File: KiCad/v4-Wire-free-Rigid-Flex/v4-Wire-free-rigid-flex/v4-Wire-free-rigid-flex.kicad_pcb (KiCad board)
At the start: 6 copper layers, 28.5 x 27 mm, 90 parts, among them J1 0475710001, J11 Conn_01x01, J12 Conn_01x01, J13 Conn_01x01, J2 Conn_01x01, J4 Conn_01x01, J5 Conn_01x01, J6 Conn_01x01, J7 Conn_01x01, J8 Conn_01x01, J9 Conn_01x01, Q1 MMBT3904LP-7B, U1 TPS62402-Q1, U2 LTC3218, U2 MAX13030EETE+, U3 ATSAME70N21A-CN, U3 TPL0102-100RUCR, U4 MAX14574EWL+, U5 LMV321IDCKR, U6 NOIP1SN0480A, U7 SiT_2.5mmx2mm, Y1 ABM8G-12.000MHZ-4Y-T3

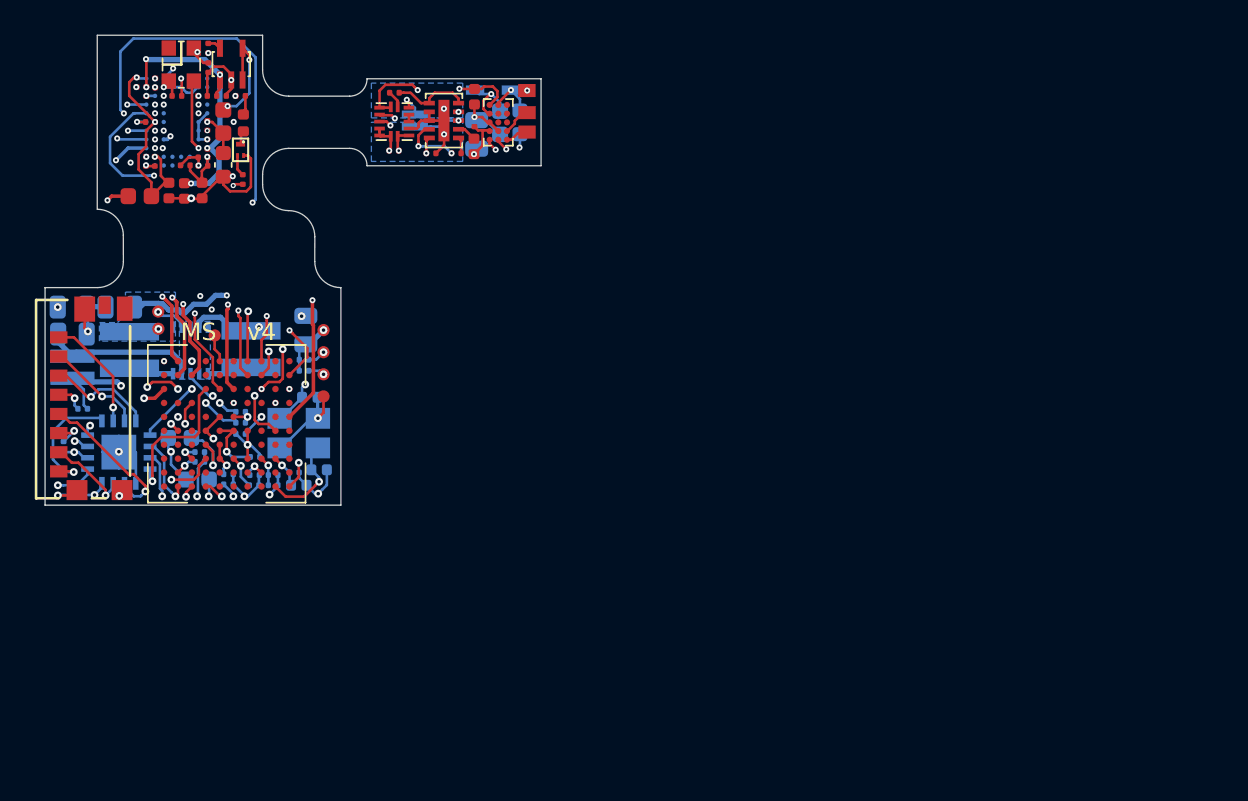
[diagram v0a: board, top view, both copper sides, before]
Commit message: Rigid-flex first draft
To do: Arrange the screw holes
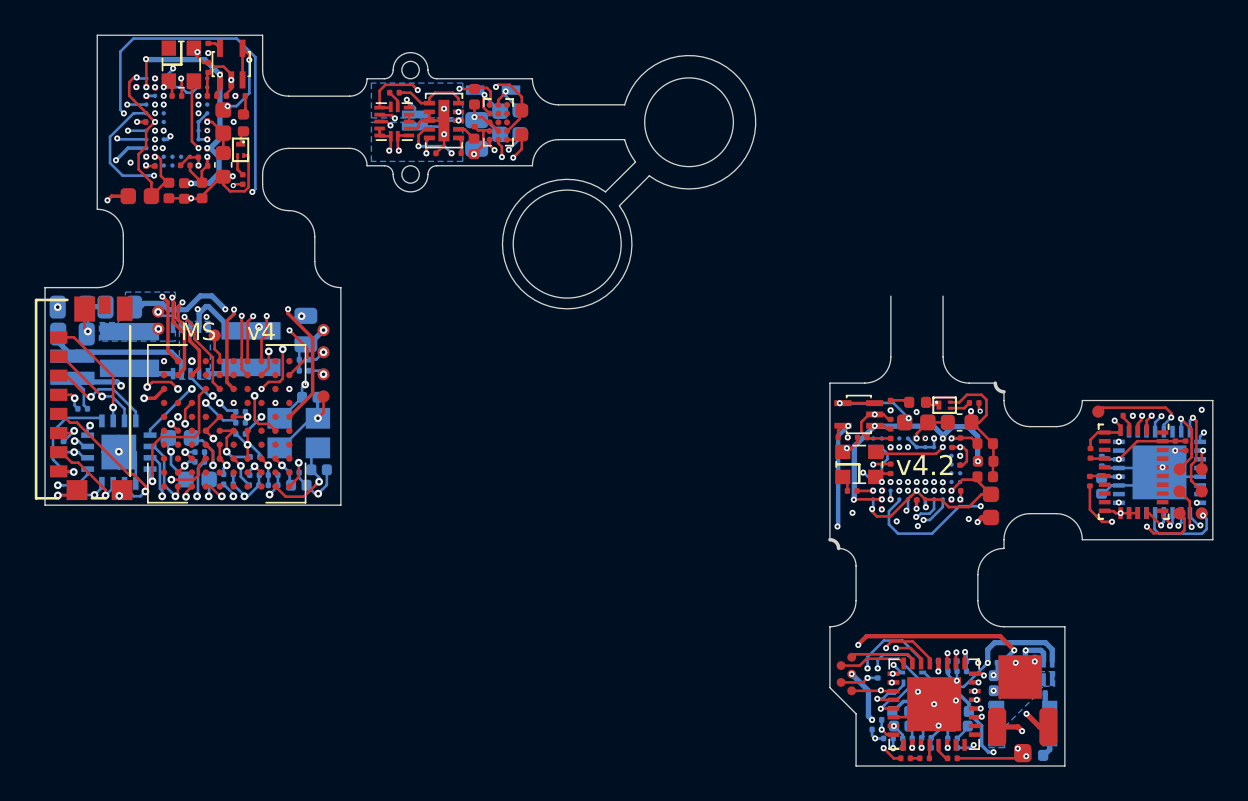
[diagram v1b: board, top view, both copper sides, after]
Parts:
- removed the J13 at (153.7, 74.6)
- added C1: GRM033R61A104ME15D, .Capacitor:C_0201_0603Metric_L, B.Cu at (186.8, 95.9)
- added C10: GRM033R61A104ME15D, .Capacitor:C_0201_0603Metric_L, F.Cu at (178.2, 94.8)
- added C11: GRM033R61A104ME15D, .Capacitor:C_0201_0603Metric_L, F.Cu at (178.6, 94.8)
- added C12: GRM033R61A104ME15D, .Capacitor:C_0201_0603Metric_L, F.Cu at (178.6, 95.8)
- added C13: GRM033R61A104ME15D, .Capacitor:C_0201_0603Metric_L, F.Cu at (174.6, 94.8)
- added C14: GRM033R61A104ME15D, .Capacitor:C_0201_0603Metric_L, F.Cu at (173.9, 97.5)
- added C15: GRM155R60J106ME15D, .Capacitor:C_0402_1005Metric_L, F.Cu at (180.1, 94.9)
- added C16: GRM033R61A104ME15D, .Capacitor:C_0201_0603Metric_L, F.Cu at (176.1, 97.8)
- added C17: GRM033R61A104ME15D, .Capacitor:C_0201_0603Metric_L, F.Cu at (173.8, 98.6)
- added C18: GRM033R61A104ME15D, .Capacitor:C_0201_0603Metric_L, F.Cu at (178.4, 97.6)
- added C19: GRM155R60J106ME15D, .Capacitor:C_0402_1005Metric_L, F.Cu at (180.1, 96.8)
- added C2: GRM155R60J475ME47D, .Capacitor:C_0402_1005Metric_L, B.Cu at (186.7, 97.3)
- added C20: GRM033R61A104ME15D, .Capacitor:C_0201_0603Metric_L, F.Cu at (177.4, 94.5)
- added C21: GRM033R61A104ME15D, .Capacitor:C_0201_0603Metric_L, F.Cu at (178.4, 98.1)
- added C22: GRM033R61A104ME15D, .Capacitor:C_0201_0603Metric_L, F.Cu at (174.4, 98.1)
- added C23: GRM155R60J106ME15D, .Capacitor:C_0402_1005Metric_L, F.Cu at (180.1, 95.9)
- added C24: GRM033R61A104ME15D, .Capacitor:C_0201_0603Metric_L, F.Cu at (176.3, 94.5)
- added C25: GRM033R61A104ME15D, .Capacitor:C_0201_0603Metric_L, F.Cu at (171.9, 94.5)
- added C26: GRM033R61A104ME15D, .Capacitor:C_0201_0603Metric_L, F.Cu at (174.6, 93.7)
- added C27: GRM188R61E475KE11D, .Capacitor:C_0603_1608Metric_L, F.Cu at (178.6, 93.6)
- added C28: GRM033R61A104ME15D, .Capacitor:C_0201_0603Metric_L, F.Cu at (173.0, 94.5)
- added C29: GRM155R60J106ME15D, .Capacitor:C_0402_1005Metric_L, B.Cu at (181.0, 108.2)
- added C30: GRM155R60J106ME15D, .Capacitor:C_0402_1005Metric_L, B.Cu at (181.0, 109.1)
- added C31: GRM033R61A104ME15D, .Capacitor:C_0201_0603Metric_L, F.Cu at (178.2, 112.9)
- added C32: GRM033R61C473KE84D, .Capacitor:C_0201_0603Metric_L, F.Cu at (176.6, 112.9)
- added C33: GRM033R61A105ME15D, .Capacitor:C_0201_0603Metric_L, B.Cu at (179.9, 107.5)
- added C34: GRM033R61A105ME15D, .Capacitor:C_0201_0603Metric_L, B.Cu at (182.1, 107.5)
- added C35: GRM033R61A105ME15D, .Capacitor:C_0201_0603Metric_L, B.Cu at (181.0, 107.5)
- added C36: GRM155R60J475ME47D, .Capacitor:C_0402_1005Metric_L, B.Cu at (176.9, 111.1)
- added C37: GRM033R61A104ME15D, .Capacitor:C_0201_0603Metric_L, B.Cu at (176.7, 112.3)
- added C38: GRM033R71A103KA01D, .Capacitor:C_0201_0603Metric_L, B.Cu at (176.7, 111.8)
- added C39: GRM155R60J475ME47D, .Capacitor:C_0402_1005Metric_L, B.Cu at (175.3, 111.1)
- added C40: GRM033R61A104ME15D, .Capacitor:C_0201_0603Metric_L, B.Cu at (175.6, 111.8)
- added C41: GRM033R71A103KA01D, .Capacitor:C_0201_0603Metric_L, B.Cu at (175.6, 112.3)
- added C42: GRM033R61A105ME15D, .Capacitor:C_0201_0603Metric_L, B.Cu at (174.5, 112.4)
- added C43: GRM155R60J106ME15D, .Capacitor:C_0402_1005Metric_L, B.Cu at (178.6, 111.1)
- added C44: GRM033R61A104ME15D, .Capacitor:C_0201_0603Metric_L, B.Cu at (178.2, 111.8)
- added C45: GRM033R71A103KA01D, .Capacitor:C_0201_0603Metric_L, B.Cu at (178.2, 112.3)
- added C46: GRM033R61A104ME15D, .Capacitor:C_0201_0603Metric_L, B.Cu at (178.7, 107.9)
- added C47: GRM033R71A103KA01D, .Capacitor:C_0201_0603Metric_L, B.Cu at (178.7, 107.3)
- added C48: GRM033R61A104ME15D, .Capacitor:C_0201_0603Metric_L, B.Cu at (177.6, 107.3)
- added C49: GRM033R71A103KA01D, .Capacitor:C_0201_0603Metric_L, B.Cu at (177.6, 107.9)
- added C51: GRM033R61A104ME15D, .Capacitor:C_0201_0603Metric_L, F.Cu at (186.1, 95.4)
- added C52: GRM033R61A104ME15D, .Capacitor:C_0201_0603Metric_L, F.Cu at (189.3, 93.3)
- added C53: GRM033R71A103KA01D, .Capacitor:C_0201_0603Metric_L, F.Cu at (191.0, 95.0)
- added C54: GRM033R61A104ME15D, .Capacitor:C_0201_0603Metric_L, F.Cu at (191.6, 95.0)
- added D3: VLMS1500-GS08, LED_SMD:LED_0402_1005Metric, F.Cu at (176.2, 92.5)
- added HOLE: Conn_1x1_250x750_Pad, .Connector:Conn_1x1_100x100_Pad, F.Cu at (147.0, 79.4)
- added HOLE: Conn_1x1_250x750_Pad, .Connector:Conn_1x1_100x100_Pad, F.Cu at (147.0, 73.4)
- added J1: DNL, .Connector:Conn_1x1_700_Circular_Pad, F.Cu at (192.5, 96.3)
- added J17: U.FL-R-SMT-1(10), .Connector:U-FL-R-SMT, F.Cu at (182.2, 111.1)
- added J2: DNL, .Connector:Conn_1x1_700_Circular_Pad, F.Cu at (191.2, 97.6)
- added J3: DNL, .Connector:Conn_1x1_700_Circular_Pad, F.Cu at (191.2, 96.3)
- added J4: DNL, .Connector:Conn_1x1_700_Circular_Pad, F.Cu at (192.5, 98.9)
- added J5: DNL, .Connector:Conn_1x1_700_Circular_Pad, F.Cu at (192.5, 97.6)
- added J6: DNL, .Connector:Conn_1x1_700_Circular_Pad, F.Cu at (191.2, 98.9)
- added J9: DNL, .Connector:Conn_1x1_700_Circular_Pad, F.Cu at (186.6, 93.0)
- added J_coax_gnd1: DNL, .Connector:Conn_1x1_100x100_Pad, F.Cu at (182.1, 108.3)
- added J_extra1: DNL, .Connector:B2B_Flex_05_Dual_Row_38milx24mil_Pad_20mil_copy, F.Cu at (172.4, 107.1)
- added L2: BLM18PG471SN1D, .Inductor:L_0603_1608Metric_L, F.Cu at (180.4, 98.4)
- added L3: BLM18PG471SN1D, .Inductor:L_0603_1608Metric_L, F.Cu at (176.1, 93.6)
- added L4: BLM15HD102SN1D, Inductor_SMD:L_0402_1005Metric, B.Cu at (182.9, 112.8)
- added L5: ADL3225V-470MT-TL000, .Inductor:L_1210_3225Metric_L, B.Cu at (182.2, 110.9)
- added L6: BLM15HD102SN1D, Inductor_SMD:L_0402_1005Metric, B.Cu at (175.2, 110.2)
- added L7: BLM15HD102SN1D, Inductor_SMD:L_0402_1005Metric, B.Cu at (178.6, 110.2)
- added Q1: MMBT3904LP-7B, .Transistor:TRXDFN3_101X61X53L25X15N, F.Cu at (177.7, 92.6)
- added R10: ERJ-1GNF1002C, .Resistor:R_0201_0603Metric_ERJ_L, B.Cu at (173.8, 111.3)
- added R11: ERJ-1GNF1003C, .Resistor:R_0201_0603Metric_ERJ_L, B.Cu at (173.8, 110.7)
- added R12: ERJ-1GNF1002C, .Resistor:R_0201_0603Metric_ERJ_L, B.Cu at (174.5, 111.8)
- added R15: ERJ-1GNF1002C, .Resistor:R_0201_0603Metric_ERJ_L, F.Cu at (188.3, 93.3)
- added R16: ERJ-1GNF1002C, .Resistor:R_0201_0603Metric_ERJ_L, F.Cu at (186.1, 97.0)
- added R2: ERJ-1GNF1002C, .Resistor:R_0201_0603Metric_ERJ_L, B.Cu at (173.3, 108.0)
- added R3: ERJ-1GNF1002C, .Resistor:R_0201_0603Metric_ERJ_L, B.Cu at (173.9, 108.0)
- added R4: ERJ-1GNF1801C, .Resistor:R_0201_0603Metric_ERJ_L, F.Cu at (174.6, 92.6)
- added R5: ERJ-1GNF1001C, .Resistor:R_0201_0603Metric_ERJ_L, F.Cu at (179.4, 92.5)
- added R6: DNL, .Resistor:R_0201_0603Metric_ERJ_L, F.Cu at (172.4, 97.6)
- added R7: ERJ-1GNF4752C, .Resistor:R_0201_0603Metric_ERJ_L, F.Cu at (174.6, 96.3)
- added R8: ERJ-1GNF1801C, .Resistor:R_0201_0603Metric_ERJ_L, B.Cu at (183.2, 109.2)
- added R9: ERJ-1GNF49R9C, .Resistor:R_0201_0603Metric_ERJ_L, F.Cu at (175.5, 112.9)
- added U1: ATmega328-MU, .Package_QFN:QFN_33_P50_500X500X80L40X24T310L, B.Cu at (190.1, 96.5)
- added U10: BNO055, Package_LGA:LGA-28_5.2x3.8mm_P0.5mm, F.Cu at (188.6, 96.5)
- added U11: PCA9509AGM, .Package_QFN:XQFN8, B.Cu at (175.9, 108.0)
- added U5: LMV321IDCKR, .Package_SOT:SOT_23-5P65_210X110L36X22L, F.Cu at (172.8, 93.2)
- added U6: NOIP1SP0480A, .Package_BGA:BGA88CP50_8X11_493X613X75B25, B.Cu at (176.1, 96.3)
- added U7: SG-210STF 66.6667ML3, .Oscillator:OSC_CC250X200X80L70X75L, F.Cu at (172.8, 96.0)
- added U8: TLV7103318DSER, .Package_SON:SON_6_P50_150X150X80L50X25L, B.Cu at (183.4, 107.9)
- added U9: DS90UB913ATRTVTQ1, .Package_QFN:QFN_33_P50_500X500X80L40X24T310L, F.Cu at (177.1, 109.8)
- C5, C7: value GRM155R60J475ME87D -> GRM155R60J475ME47D
- C50: value GRM033R61A104ME15D -> GRM21BR61A476ME15L
- C9: value 100nF 100V 0603 -> GRJ188R72A104KE11D
- D2: value BAS316 -> BAS316-TP
- J11, J12: value Conn_01x01 -> DNL
- L1: value LQM18PN3R3MGHD -> MBKK1608T3R3M
- R1: value ERJ-1GEF1022C -> ERJ-1GNF1022C
- moved J12 0.34 mm to (153.4, 77.1)
- moved J11 0.33 mm to (153.4, 75.7)
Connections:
- U2 pad 4: /LED_ENT -> /LED-EWL/ENT1
- U3 pad 10: /SCL -> /LED-EWL/SCL_3V3
- U3 pad 9: /SDA -> /LED-EWL/SDA_3V3
- U4 pad A1: /SDA -> /LED-EWL/SDA_3V3
- U4 pad B1: /SCL -> /LED-EWL/SCL_3V3
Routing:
- net GND: track 102.0 -> 231.7 mm, vias 41 -> 78
- net +1V8: track 50.1 -> 126.1 mm, vias 17 -> 34
- net +3V3: track 65.4 -> 136.9 mm, vias 14 -> 25
- net /IMU/I2C_SDA: track 0.00 -> 42.2 mm, vias 0 -> 2
- net /LED-EWL/SDA_3V3: track 0.00 -> 41.1 mm, vias 0 -> 3
- net /IMU/I2C_SCL: track 0.00 -> 39.7 mm, vias 0 -> 2
- net /LED-EWL/SCL_3V3: track 0.00 -> 38.7 mm, vias 0 -> 3
- net /MCU/SCK: track 0.00 -> 38.5 mm, vias 0 -> 3
- net /LED-EWL/ENT1: track 0.00 -> 29.2 mm, vias 0 -> 2
- net +5V: track 0.79 -> 26.1 mm, vias 0 -> 4
- net /MCU/MISO: track 0.00 -> 24.8 mm, vias 0 -> 2
- net /MCU/TRIGGER0: track 0.00 -> 21.5 mm, vias 0 -> 2
- net /MCU/MOSI: track 0.00 -> 21.5 mm, vias 0 -> 2
- net /MCU/MONITOR0: track 0.00 -> 21.2 mm, vias 0 -> 2
- net /MCU/RESET_N: track 0.00 -> 19.5 mm, vias 0 -> 2
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- added copper zone on B.Cu, net +5V
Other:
- board size 28.5 x 27 mm -> 67.1 x 42 mm
- net class Default: clearance 0.0889 -> 0.1016; trace_width 0.0889 -> 0.1016; via_dia 0.45 -> 0.3; via_drill 0.2 -> 0.15
- rule trace_clearance: 0.0889 -> 0.1016
- rule trace_min: 0.0889 -> 0.1016
- rule via_min_drill: 0.2 -> 0.15
- rule via_min_size: 0.45 -> 0.3
- board text added: "1mm longer than theoretical length. 0.5mm shorter than previous"
- board text added: "Make sure arcs on flex are not covered by mask"
- board text added: "v4.2"
